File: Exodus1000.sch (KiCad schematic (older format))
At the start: 2 parts, among them J3 Conn_01x02, U5 IS42S16400J-xT

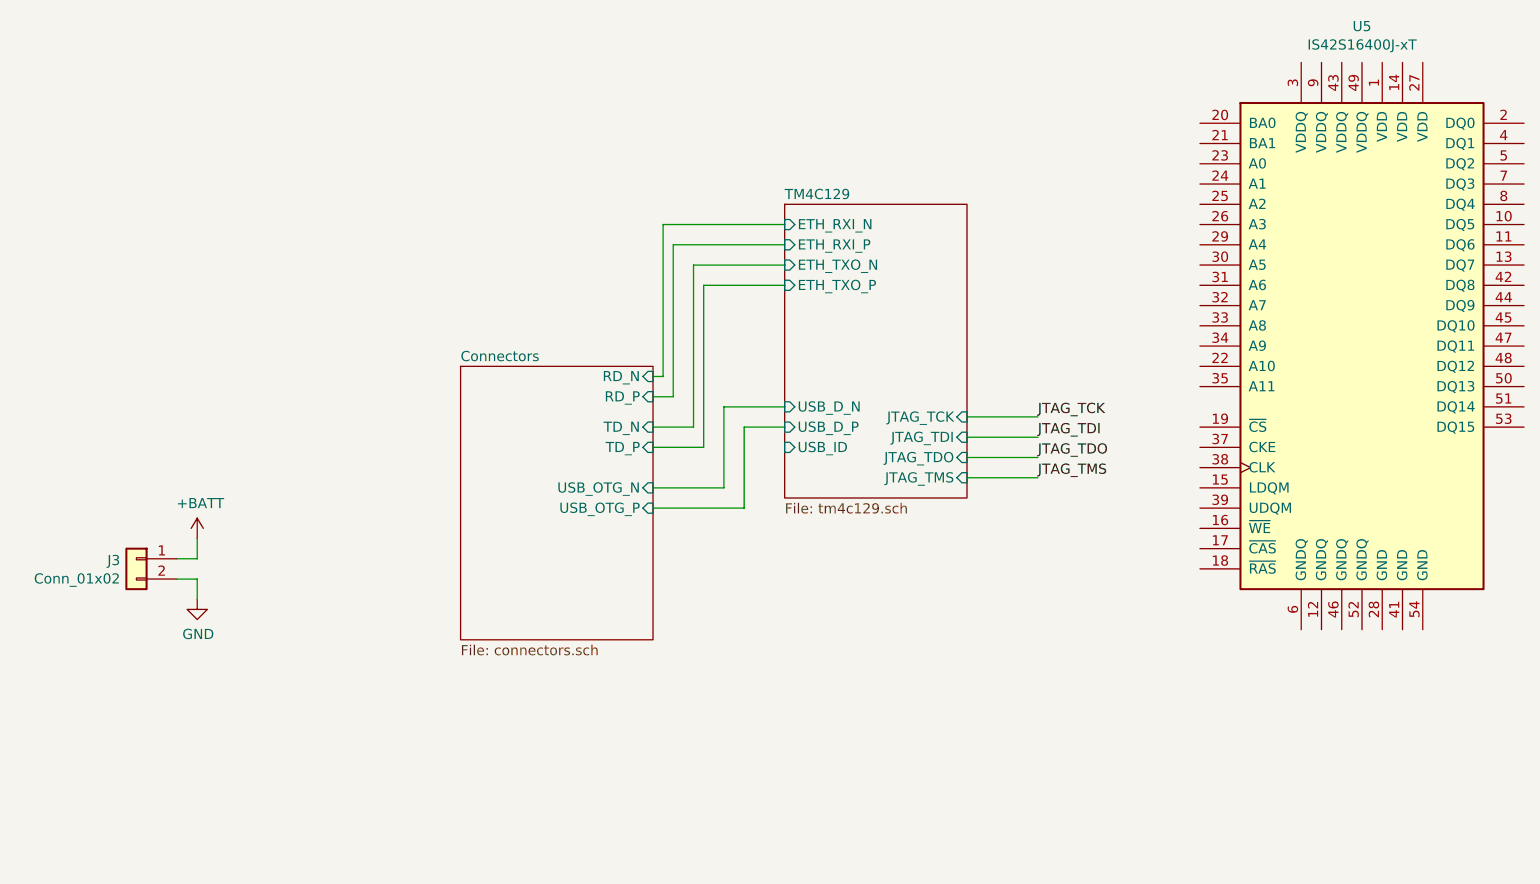
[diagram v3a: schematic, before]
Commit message: schematics for expansion slots and memory
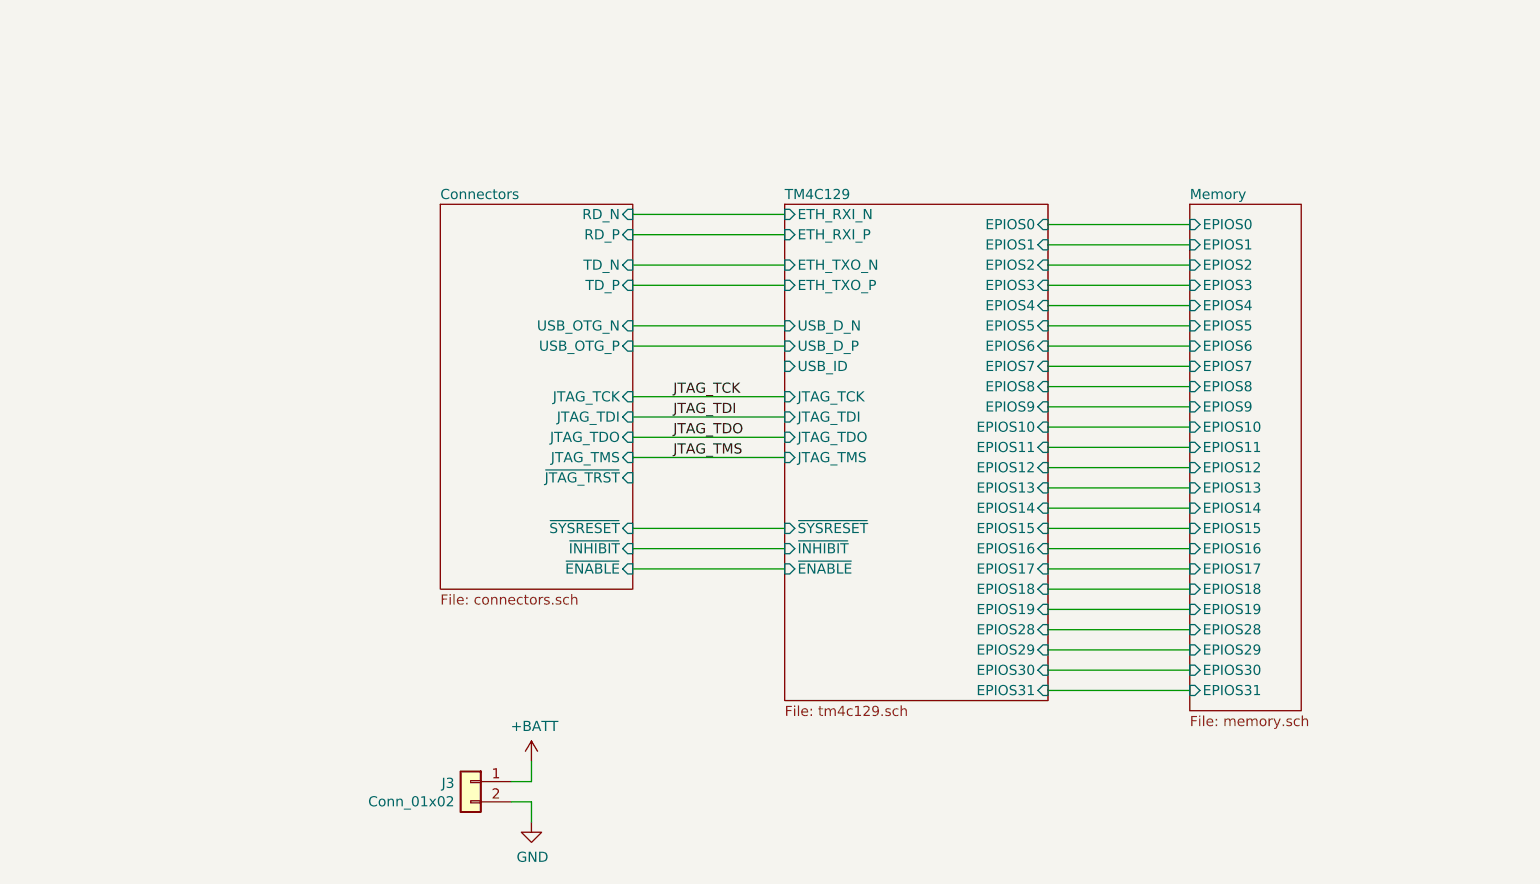
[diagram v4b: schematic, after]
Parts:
- removed U5: IS42S16400J-xT, Package_SO:TSOP-II-54_22.2x10.16mm_P0.8mm, symbol Memory_RAM:IS42S16400J-xT
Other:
- moved on the sheet: J3
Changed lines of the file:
@@
 $Descr A4 11693 8268
 encoding utf-8
-Sheet 1 5
+Sheet 1 10
 Title "Exodus1000"
 Date "2019-03-16"
@@
 $EndDescr
 $Sheet
-S 5450 2050 900  1450
+S 5450 2050 1300 2450
 U 5C80AE96
 F0 "TM4C129" 50
 F1 "tm4c129.sch" 50
-F2 "ETH_RXI_N" I L 5450 2150 50
-F3 "ETH_RXI_P" I L 5450 2250 50
+F2 "ETH_RXI_N" I L 5450 2100 50
+F3 "ETH_RXI_P" I L 5450 2200 50
 F4 "ETH_TXO_N" I L 5450 2350 50
 F5 "ETH_TXO_P" I L 5450 2450 50
-F6 "JTAG_TCK" I R 6350 3100 50
-F7 "JTAG_TMS" I R 6350 3400 50
-F8 "JTAG_TDI" I R 6350 3200 50
-F9 "JTAG_TDO" I R 6350 3300 50
-F10 "USB_D_N" I L 5450 3050 50
-F11 "USB_D_P" I L 5450 3150 50
-F12 "USB_ID" I L 5450 3250 50
+F6 "JTAG_TCK" I L 5450 3000 50
+F7 "JTAG_TMS" I L 5450 3300 50
+F8 "JTAG_TDI" I L 5450 3100 50
+F9 "JTAG_TDO" I L 5450 3200 50
+F10 "USB_D_N" I L 5450 2650 50
+F11 "USB_D_P" I L 5450 2750 50
+F12 "USB_ID" I L 5450 2850 50
+F13 "EPIOS0" I R 6750 2150 50
+F14 "EPIOS1" I R 6750 2250 50
+F15 "EPIOS2" I R 6750 2350 50
+F16 "EPIOS3" I R 6750 2450 50
+F17 "EPIOS4" I R 6750 2550 50
+F18 "EPIOS5" I R 6750 2650 50
+F19 "EPIOS6" I R 6750 2750 50
+F20 "EPIOS7" I R 6750 2850 50
+F21 "EPIOS8" I R 6750 2950 50
+F22 "EPIOS9" I R 6750 3050 50
+F23 "EPIOS10" I R 6750 3150 50
+F24 "EPIOS11" I R 6750 3250 50
+F25 "EPIOS12" I R 6750 3350 50
+F26 "EPIOS13" I R 6750 3450 50
+F27 "EPIOS14" I R 6750 3550 50
+F28 "EPIOS15" I R 6750 3650 50
+F29 "EPIOS16" I R 6750 3750 50
+F30 "EPIOS17" I R 6750 3850 50
+F31 "EPIOS18" I R 6750 3950 50
+F32 "EPIOS19" I R 6750 4050 50
+F33 "EPIOS28" I R 6750 4150 50
+F34 "EPIOS29" I R 6750 4250 50
+F35 "EPIOS30" I R 6750 4350 50
+F36 "EPIOS31" I R 6750 4450 50
+F37 "~ENABLE" I L 5450 3850 50
+F38 "~INHIBIT" I L 5450 3750 50
+F39 "~SYSRESET" I L 5450 3650 50
 $EndSheet
 $Sheet
-S 3850 2850 950  1350
+S 3750 2050 950  1900
 U 5C8128A2
 F0 "Connectors" 50
 F1 "connectors.sch" 50
-F2 "USB_OTG_N" I R 4800 3450 50
-F3 "USB_OTG_P" I R 4800 3550 50
-F4 "TD_P" I R 4800 3250 50
-F5 "TD_N" I R 4800 3150 50
-F6 "RD_P" I R 4800 3000 50
-F7 "RD_N" I R 4800 2900 50
+F2 "USB_OTG_N" I R 4700 2650 50
+F3 "USB_OTG_P" I R 4700 2750 50
+F4 "TD_P" I R 4700 2450 50
+F5 "TD_N" I R 4700 2350 50
+F6 "RD_P" I R 4700 2200 50
+F7 "RD_N" I R 4700 2100 50
+F8 "~ENABLE" I R 4700 3850 50
+F9 "~INHIBIT" I R 4700 3750 50
+F10 "~SYSRESET" I R 4700 3650 50
+F11 "~JTAG_TRST" I R 4700 3400 50
+F12 "JTAG_TMS" I R 4700 3300 50
+F13 "JTAG_TDO" I R 4700 3200 50
+F14 "JTAG_TDI" I R 4700 3100 50
+F15 "JTAG_TCK" I R 4700 3000 50
 $EndSheet
-Wire Wire Line
-	4800 3450 5150 3450
-Wire Wire Line
-	5150 3450 5150 3050
-Wire Wire Line
-	5150 3050 5450 3050
-Wire Wire Line
-	5450 3150 5250 3150
-Wire Wire Line
-	5250 3150 5250 3550
-Wire Wire Line
-	5250 3550 4800 3550
-Wire Wire Line
-	4800 2900 4850 2900
-Wire Wire Line
-	4850 2900 4850 2150
-Wire Wire Line
-	4850 2150 5450 2150
-Wire Wire Line
-	5450 2250 4900 2250
-Wire Wire Line
-	4900 2250 4900 3000
-Wire Wire Line
-	4900 3000 4800 3000
-Wire Wire Line
-	4800 3150 5000 3150
-Wire Wire Line
-	5000 3150 5000 2350
-Wire Wire Line
-	5000 2350 5450 2350
-Wire Wire Line
-	5450 2450 5050 2450
-Wire Wire Line
-	5050 2450 5050 3250
-Wire Wire Line
-	5050 3250 4800 3250
-Wire Wire Line
-	6350 3100 6700 3100
-Wire Wire Line
-	6350 3200 6700 3200
-Wire Wire Line
-	6350 3300 6700 3300
-Wire Wire Line
-	6350 3400 6700 3400
-Text Label 6700 3100 0    50   ~ 0
+Text Label 4900 3000 0    50   ~ 0
 JTAG_TCK
-Text Label 6700 3200 0    50   ~ 0
+Text Label 4900 3100 0    50   ~ 0
 JTAG_TDI
-Text Label 6700 3300 0    50   ~ 0
+Text Label 4900 3200 0    50   ~ 0
 JTAG_TDO
-Text Label 6700 3400 0    50   ~ 0
+Text Label 4900 3300 0    50   ~ 0
 JTAG_TMS
 $Comp
 L Connector_Generic:Conn_01x02 J3
 U 1 1 5C872DE6
-P 2250 3800
-F 0 "J3" H 2330 3792 50  0000 L CNN
-F 1 "Conn_01x02" H 2330 3701 50  0000 L CNN
-F 2 "Connector_PinHeader_2.54mm:PinHeader_1x02_P2.54mm_Horizontal" H 2250 3800 50  0001 C CNN
-F 3 "~" H 2250 3800 50  0001 C CNN
-	1    2250 3800
+P 3900 4900
+F 0 "J3" H 3980 4892 50  0000 L CNN
+F 1 "Conn_01x02" H 3980 4801 50  0000 L CNN
+F 2 "Connector_PinHeader_2.54mm:PinHeader_1x02_P2.54mm_Horizontal" H 3900 4900 50  0001 C CNN
+F 3 "~" H 3900 4900 50  0001 C CNN
+	1    3900 4900
 	-1   0    0    -1
 $EndComp
 Wire Wire Line
-	2450 3800 2550 3800
-Wire Wire Line
-	2550 3800 2550 3700
-Wire Wire Line
-	2450 3900 2550 3900
-Wire Wire Line
-	2550 3900 2550 4000
+	4100 4900 4200 4900
+Wire Wire Line
+	4200 4900 4200 4800
+Wire Wire Line
+	4100 5000 4200 5000
+Wire Wire Line
+	4200 5000 4200 5100
 $Comp
 L power:GND #PWR0149
 U 1 1 5C8F5DB2
-P 2550 4000
-F 0 "#PWR0149" H 2550 3750 50  0001 C CNN
-F 1 "GND" H 2555 3827 50  0000 C CNN
-F 2 "" H 2550 4000 50  0001 C CNN
-F 3 "" H 2550 4000 50  0001 C CNN
-	1    2550 4000
+P 4200 5100
+F 0 "#PWR0149" H 4200 4850 50  0001 C CNN
+F 1 "GND" H 4205 4927 50  0000 C CNN
+F 2 "" H 4200 5100 50  0001 C CNN
+F 3 "" H 4200 5100 50  0001 C CNN
+	1    4200 5100
 	1    0    0    -1
 $EndComp
@@
 L power:+BATT #PWR0150
 U 1 1 5C8F5ED8
-P 2550 3700
-F 0 "#PWR0150" H 2550 3550 50  0001 C CNN
-F 1 "+BATT" H 2565 3873 50  0000 C CNN
-F 2 "" H 2550 3700 50  0001 C CNN
-F 3 "" H 2550 3700 50  0001 C CNN
-	1    2550 3700
+P 4200 4800
+F 0 "#PWR0150" H 4200 4650 50  0001 C CNN
+F 1 "+BATT" H 4215 4973 50  0000 C CNN
+F 2 "" H 4200 4800 50  0001 C CNN
+F 3 "" H 4200 4800 50  0001 C CNN
+	1    4200 4800
 	1    0    0    -1
 $EndComp
-$Comp
-L Memory_RAM:IS42S16400J-xT U5
-U 1 1 5CA3FBF0
-P 8300 2750
-F 0 "U5" H 8300 4328 50  0000 C CNN
-F 1 "IS42S16400J-xT" H 8300 4237 50  0000 C CNN
-F 2 "Package_SO:TSOP-II-54_22.2x10.16mm_P0.8mm" H 8300 2750 50  0001 C CNN
-F 3 "http://www.issi.com/WW/pdf/42-45S16400J.pdf" H 7700 4000 50  0001 C CNN
-	1    8300 2750
-	1    0    0    -1
-$EndComp
+Wire Wire Line
+	4700 2100 5450 2100
+Wire Wire Line
+	4700 2200 5450 2200
+Wire Wire Line
+	4700 2350 5450 2350
+Wire Wire Line
+	4700 2450 5450 2450
+Wire Wire Line
+	4700 2650 5450 2650
+Wire Wire Line
+	4700 2750 5450 2750
+Wire Wire Line
+	4700 3000 5450 3000
+Wire Wire Line
+	5450 3100 4700 3100
+Wire Wire Line
+	4700 3200 5450 3200
+Wire Wire Line
+	5450 3300 4700 3300
+$Sheet
+S 7450 2050 550  2500
+U 5CAC3D25
+F0 "Memory" 50
+F1 "memory.sch" 50
+F2 "EPIOS13" I L 7450 3450 50
+F3 "EPIOS14" I L 7450 3550 50
+F4 "EPIOS0" I L 7450 2150 50
+F5 "EPIOS1" I L 7450 2250 50
+F6 "EPIOS2" I L 7450 2350 50
+F7 "EPIOS3" I L 7450 2450 50
+F8 "EPIOS4" I L 7450 2550 50
+F9 "EPIOS5" I L 7450 2650 50
+F10 "EPIOS6" I L 7450 2750 50
+F11 "EPIOS7" I L 7450 2850 50
+F12 "EPIOS8" I L 7450 2950 50
+F13 "EPIOS9" I L 7450 3050 50
+F14 "EPIOS10" I L 7450 3150 50
+F15 "EPIOS11" I L 7450 3250 50
+F16 "EPIOS12" I L 7450 3350 50
+F17 "EPIOS15" I L 7450 3650 50
+F18 "EPIOS29" I L 7450 4250 50
+F19 "EPIOS31" I L 7450 4450 50
+F20 "EPIOS16" I L 7450 3750 50
+F21 "EPIOS17" I L 7450 3850 50
+F22 "EPIOS28" I L 7450 4150 50
+F23 "EPIOS18" I L 7450 3950 50
+F24 "EPIOS19" I L 7450 4050 50
+F25 "EPIOS30" I L 7450 4350 50
+$EndSheet
+Wire Wire Line
+	6750 2150 7450 2150
+Wire Wire Line
+	6750 2250 7450 2250
+Wire Wire Line
+	6750 2350 7450 2350
+Wire Wire Line
+	6750 2450 7450 2450
+Wire Wire Line
+	6750 2550 7450 2550
+Wire Wire Line
+	6750 2650 7450 2650
+Wire Wire Line
+	6750 2750 7450 2750
+Wire Wire Line
+	6750 2850 7450 2850
+Wire Wire Line
+	6750 2950 7450 2950
+Wire Wire Line
+	6750 3050 7450 3050
+Wire Wire Line
+	6750 3150 7450 3150
+Wire Wire Line
+	6750 3250 7450 3250
+Wire Wire Line
+	6750 3350 7450 3350
+Wire Wire Line
+	6750 3450 7450 3450
+Wire Wire Line
+	6750 3550 7450 3550
+Wire Wire Line
+	6750 3650 7450 3650
+Wire Wire Line
+	6750 3750 7450 3750
+Wire Wire Line
+	6750 3850 7450 3850
+Wire Wire Line
+	6750 3950 7450 3950
+Wire Wire Line
+	6750 4050 7450 4050
+Wire Wire Line
+	6750 4150 7450 4150
+Wire Wire Line
+	6750 4250 7450 4250
+Wire Wire Line
+	6750 4350 7450 4350
+Wire Wire Line
+	6750 4450 7450 4450
+Wire Wire Line
+	4700 3650 5450 3650
+Wire Wire Line
+	4700 3750 5450 3750
+Wire Wire Line
+	4700 3850 5450 3850
 $EndSCHEMATC

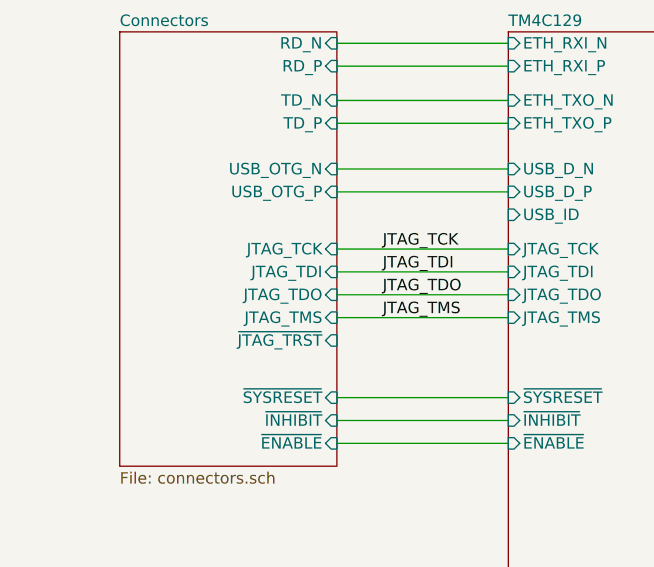
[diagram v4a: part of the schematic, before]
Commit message: fixing up the jtag connections. Should be good now
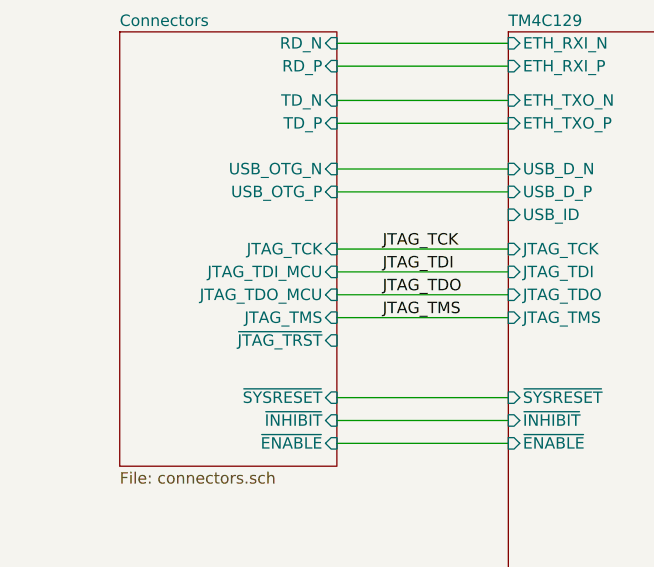
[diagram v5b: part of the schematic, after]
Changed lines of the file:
@@
 F11 "~JTAG_TRST" I R 4700 3400 50
 F12 "JTAG_TMS" I R 4700 3300 50
-F13 "JTAG_TDO" I R 4700 3200 50
-F14 "JTAG_TDI" I R 4700 3100 50
-F15 "JTAG_TCK" I R 4700 3000 50
+F13 "JTAG_TCK" I R 4700 3000 50
+F14 "JTAG_TDI_MCU" I R 4700 3100 50
+F15 "JTAG_TDO_MCU" I R 4700 3200 50
 $EndSheet
 Text Label 4900 3000 0    50   ~ 0

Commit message: almost done with draft 1 of layout
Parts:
- added D1: LED, LED_SMD:LED_0603_1608Metric, symbol Device:LED
- added R30: R_Small, Resistor_SMD:R_0603_1608Metric, symbol Device:R_Small
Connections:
- net +BATT: now also D1.2 (A)
- net GND: now also R30.1
- new net: D1.1 (K), R30.2
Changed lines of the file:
@@
 Text Label 4900 3300 0    50   ~ 0
 JTAG_TMS
-$Comp
-L Connector_Generic:Conn_01x02 J3
-U 1 1 5C872DE6
-P 3900 4900
-F 0 "J3" H 3980 4892 50  0000 L CNN
-F 1 "Conn_01x02" H 3980 4801 50  0000 L CNN
-F 2 "Connector_PinHeader_2.54mm:PinHeader_1x02_P2.54mm_Horizontal" H 3900 4900 50  0001 C CNN
-F 3 "~" H 3900 4900 50  0001 C CNN
-	1    3900 4900
-	-1   0    0    -1
-$EndComp
 Wire Wire Line
 	4100 4900 4200 4900
@@
 Wire Wire Line
 	4700 3850 5450 3850
+$Comp
+L Device:LED D1
+U 1 1 5CD7F8C0
+P 4550 4900
+F 0 "D1" H 4542 4645 50  0000 C CNN
+F 1 "LED" H 4542 4736 50  0000 C CNN
+F 2 "LED_SMD:LED_0603_1608Metric" H 4550 4900 50  0001 C CNN
+F 3 "~" H 4550 4900 50  0001 C CNN
+	1    4550 4900
+	-1   0    0    1
+$EndComp
+Wire Wire Line
+	4200 4900 4400 4900
+Connection ~ 4200 4900
+$Comp
+L Device:R_Small R30
+U 1 1 5CD80817
+P 4800 5050
+F 0 "R30" H 4741 5004 50  0000 R CNN
+F 1 "R_Small" H 4741 5095 50  0000 R CNN
+F 2 "Resistor_SMD:R_0603_1608Metric" H 4800 5050 50  0001 C CNN
+F 3 "~" H 4800 5050 50  0001 C CNN
+	1    4800 5050
+	-1   0    0    1
+$EndComp
+Wire Wire Line
+	4700 4900 4800 4900
+Wire Wire Line
+	4800 4900 4800 4950
+$Comp
+L power:GND #PWR0184
+U 1 1 5CD81450
+P 4800 5250
+F 0 "#PWR0184" H 4800 5000 50  0001 C CNN
+F 1 "GND" H 4805 5077 50  0000 C CNN
+F 2 "" H 4800 5250 50  0001 C CNN
+F 3 "" H 4800 5250 50  0001 C CNN
+	1    4800 5250
+	1    0    0    -1
+$EndComp
+Wire Wire Line
+	4800 5150 4800 5250
+$Comp
+L Connector_Generic:Conn_01x02 J3
+U 1 1 5C872DE6
+P 3900 4900
+F 0 "J3" H 3980 4892 50  0000 L CNN
+F 1 "Conn_01x02" H 3980 4801 50  0000 L CNN
+F 2 "Connector_PinHeader_2.54mm:PinHeader_1x02_P2.54mm_Horizontal" H 3900 4900 50  0001 C CNN
+F 3 "~" H 3900 4900 50  0001 C CNN
+	1    3900 4900
+	-1   0    0    -1
+$EndComp
 $EndSCHEMATC
